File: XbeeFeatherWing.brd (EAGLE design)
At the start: 124.5 x 66 mm, 18 parts, among them U2 XBEE-1B3

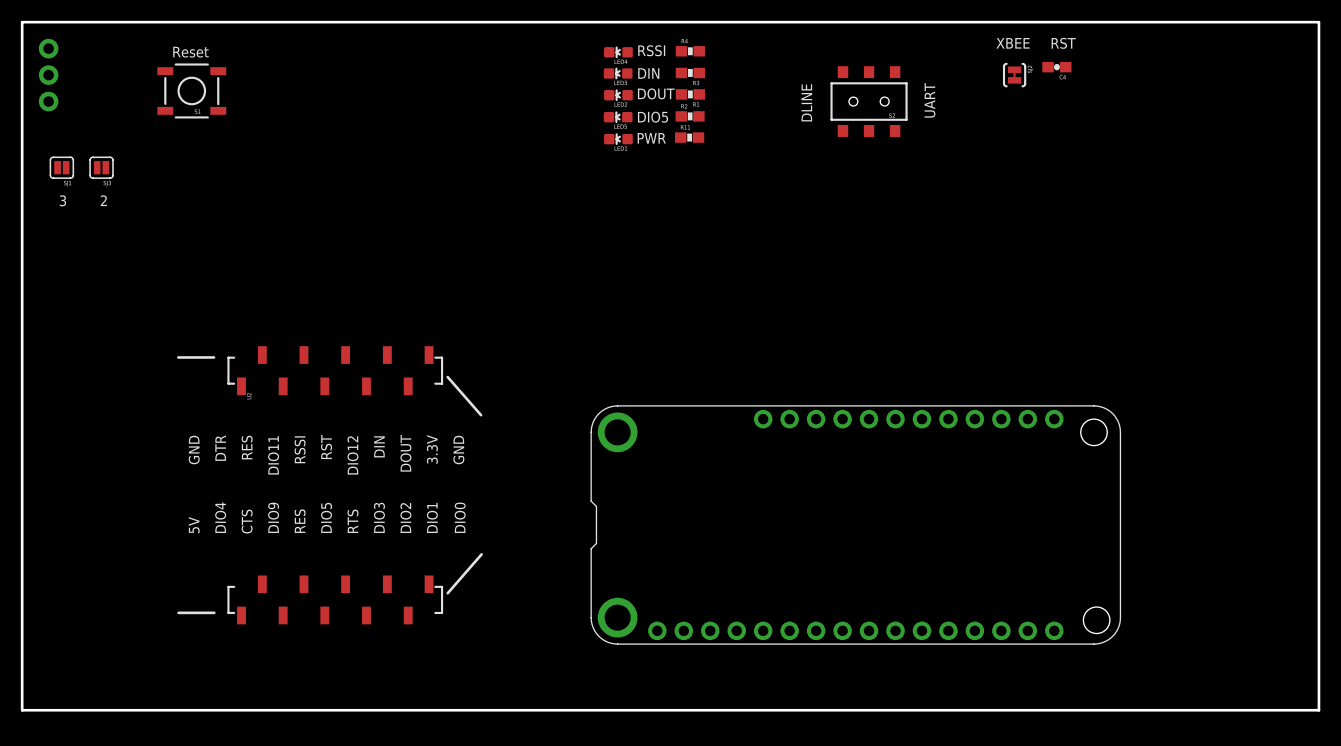
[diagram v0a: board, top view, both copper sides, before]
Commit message: changed xbee to adafruit footprint
the sparkfun footprint was smd, needed THT pins
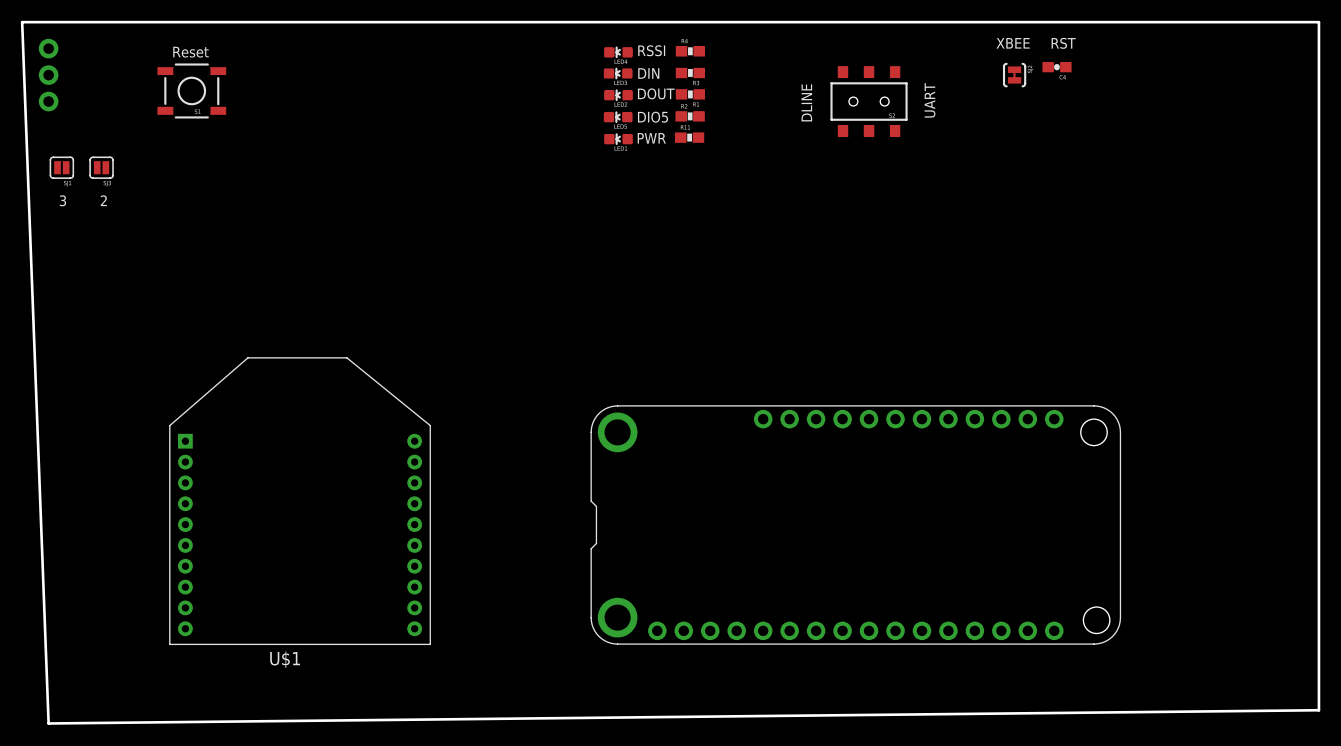
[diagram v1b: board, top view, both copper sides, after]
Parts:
- removed U2: XBEE-1B3, SparkFun:XBEE-SMD
- added U$1: XBEE, adafruit:XBEE
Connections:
- new net N$8: U$1.17
- net 3.3V: now also U$1.1; no longer U2.1
- net DIN: now also U$1.3; no longer U2.3
- net DIO3: no longer U2.17
- net DIO5: now also U$1.15; no longer U2.15
- net DOUT: now also U$1.2; no longer U2.2
- net GND: now also U$1.10; no longer U2.10
- net RSSI: now also U$1.6; no longer U2.6
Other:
- board size 124.5 x 66 mm -> 124.5 x 67.3 mm
- board text removed: "3.3V"
- board text removed: "5V"
- board text removed: "CTS"
- board text removed: "DIO0"
- board text removed: "DIO1"
- board text removed: "DIO11"
- board text removed: "DIO12"
- board text removed: "DIO2"
- board text removed: "DIO3"
- board text removed: "DIO4"
- board text removed: "DIO9"
- board text removed: "DTR"
- board text removed: "GND"
- board text removed: "RES"
- board text removed: "RTS"
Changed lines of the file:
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@@
 <board>
 <plain>
-<wire x1="0" y1="-6.35" x2="0" y2="59.69" width="0.254" layer="20"/>
+<wire x1="2.54" y1="-7.62" x2="0" y2="59.69" width="0.254" layer="20"/>
 <wire x1="0" y1="59.69" x2="124.46" y2="59.69" width="0.254" layer="20"/>
 <wire x1="124.46" y1="59.69" x2="124.46" y2="-6.35" width="0.254" layer="20"/>
-<wire x1="124.46" y1="-6.35" x2="0" y2="-6.35" width="0.254" layer="20"/>
-<wire x1="40.8432" y1="25.6286" x2="44.0436" y2="21.971" width="0.254" layer="21"/>
-<wire x1="40.8432" y1="4.8768" x2="44.0944" y2="8.6106" width="0.254" layer="21"/>
-<wire x1="18.4404" y1="2.9972" x2="15.0114" y2="2.9972" width="0.254" layer="21"/>
-<wire x1="18.415" y1="27.5082" x2="14.986" y2="27.5082" width="0.254" layer="21"/>
-<text x="42.545" y="10.541" size="1.016" layer="21" font="vector" ratio="15" rot="R90">DIO0</text>
-<text x="39.878" y="10.541" size="1.016" layer="21" font="vector" ratio="15" rot="R90">DIO1</text>
-<text x="37.338" y="10.541" size="1.016" layer="21" font="vector" ratio="15" rot="R90">DIO2</text>
-<text x="34.798" y="10.541" size="1.016" layer="21" font="vector" ratio="15" rot="R90">DIO3</text>
-<text x="32.258" y="10.541" size="1.016" layer="21" font="vector" ratio="15" rot="R90">RTS</text>
-<text x="29.718" y="10.541" size="1.016" layer="21" font="vector" ratio="15" rot="R90">DIO5</text>
-<text x="27.178" y="10.541" size="1.016" layer="21" font="vector" ratio="15" rot="R90">RES</text>
-<text x="24.638" y="10.541" size="1.016" layer="21" font="vector" ratio="15" rot="R90">DIO9</text>
-<text x="22.098" y="10.541" size="1.016" layer="21" font="vector" ratio="15" rot="R90">CTS</text>
-<text x="19.558" y="10.541" size="1.016" layer="21" font="vector" ratio="15" rot="R90">DIO4</text>
-<text x="17.018" y="10.541" size="1.016" layer="21" font="vector" ratio="15" rot="R90">5V</text>
-<text x="16.002" y="20.066" size="1.016" layer="21" font="vector" ratio="15" rot="R270">GND</text>
-<text x="18.542" y="20.066" size="1.016" layer="21" font="vector" ratio="15" rot="R270">DTR</text>
-<text x="21.082" y="20.066" size="1.016" layer="21" font="vector" ratio="15" rot="R270">RES</text>
-<text x="23.622" y="20.066" size="1.016" layer="21" font="vector" ratio="15" rot="R270">DIO11</text>
-<text x="26.162" y="20.066" size="1.016" layer="21" font="vector" ratio="15" rot="R270">RSSI</text>
-<text x="28.702" y="20.066" size="1.016" layer="21" font="vector" ratio="15" rot="R270">RST</text>
-<text x="31.242" y="20.066" size="1.016" layer="21" font="vector" ratio="15" rot="R270">DIO12</text>
-<text x="33.782" y="20.066" size="1.016" layer="21" font="vector" ratio="15" rot="R270">DIN</text>
-<text x="36.322" y="20.066" size="1.016" layer="21" font="vector" ratio="15" rot="R270">DOUT</text>
-<text x="38.862" y="20.066" size="1.016" layer="21" font="vector" ratio="15" rot="R270">3.3V</text>
-<text x="41.402" y="20.066" size="1.016" layer="21" font="vector" ratio="15" rot="R270">GND</text>
+<wire x1="124.46" y1="-6.35" x2="2.54" y2="-7.62" width="0.254" layer="20"/>
 <text x="59.0042" y="56.4388" size="1.016" layer="21" font="vector" ratio="15" rot="SR0">RSSI</text>
 <text x="59.0042" y="54.2544" size="1.016" layer="21" font="vector" ratio="15" rot="SR0">DIN</text>
@@
 <attribute name="VALUE" value="1K" x="64.135" y="54.8132" size="1.778" layer="27" rot="R180" display="off"/>
 </element>
-<element name="U2" library="SparkFun" package="XBEE-SMD" value="XBEE-1B3" x="19.05" y="15.24" rot="R270"/>
 <element name="LED4" library="SparkFun-LED" package="LED-0603" value="Green" x="57.2262" y="56.7944" rot="R90">
 <attribute name="PROD_ID" value="DIO-00821" x="57.2262" y="56.7944" size="1.778" layer="27" rot="R90" display="off"/>
@@
 <element name="SJ3" library="SparkFun" package="SJ_2S" value="D_RX" x="7.62" y="45.72" rot="R180"/>
 <element name="MS2" library="Proto FeatherWing" package="MICROSHIELD_DIM" value="MICROSHIELD_NODIM" x="54.61" y="0"/>
+<element name="U$1" library="adafruit" package="XBEE" value="XBEE" x="26.67" y="13.97"/>
 </elements>
 <signals>
@@
 <contactref element="MS2" pad="4"/>
 <contactref element="MS2" pad="27"/>
-<contactref element="U2" pad="10"/>
+<contactref element="U$1" pad="10"/>
 <wire x1="56.3238" y1="50.5714" x2="56.3492" y2="56.7944" width="0" layer="19" extent="1-1"/>
 <wire x1="56.3492" y1="48.4632" x2="56.3238" y2="50.5714" width="0" layer="19" extent="1-1"/>
@@
 <wire x1="68.58" y1="1.27" x2="73.66" y2="21.59" width="0" layer="19" extent="1-1"/>
 <wire x1="18.8214" y1="51.181" x2="56.3238" y2="50.5714" width="0" layer="19" extent="1-1"/>
-<wire x1="21.05" y1="24.74" x2="18.8214" y2="51.181" width="0" layer="19" extent="1-1"/>
+<wire x1="15.67" y1="1.47" x2="18.8214" y2="51.181" width="0" layer="19" extent="1-1"/>
 </signal>
 <signal name="N$38">
@@
 <signal name="DIN">
 <contactref element="LED3" pad="C"/>
-<contactref element="U2" pad="3"/>
 <contactref element="S2" pad="5"/>
+<contactref element="U$1" pad="3"/>
 <wire x1="56.3238" y1="54.7624" x2="81.28" y2="54.895" width="0" layer="19" extent="1-1"/>
-<wire x1="35.05" y1="27.74" x2="56.3238" y2="54.7624" width="0" layer="19" extent="1-1"/>
+<wire x1="15.67" y1="15.47" x2="56.3238" y2="54.7624" width="0" layer="19" extent="1-1"/>
 </signal>
 <signal name="DOUT">
 <contactref element="LED2" pad="C"/>
-<contactref element="U2" pad="2"/>
 <contactref element="S2" pad="2"/>
+<contactref element="U$1" pad="2"/>
 <wire x1="56.3492" y1="52.6796" x2="81.28" y2="49.245" width="0" layer="19" extent="1-1"/>
-<wire x1="37.05" y1="24.74" x2="56.3492" y2="52.6796" width="0" layer="19" extent="1-1"/>
+<wire x1="15.67" y1="17.47" x2="56.3492" y2="52.6796" width="0" layer="19" extent="1-1"/>
 </signal>
 <signal name="3.3V">
-<contactref element="U2" pad="1"/>
 <contactref element="R11" pad="2"/>
 <contactref element="R3" pad="1"/>
 <contactref element="R1" pad="1"/>
 <contactref element="MS2" pad="2"/>
+<contactref element="U$1" pad="1"/>
 <wire x1="64.985" y1="52.7558" x2="64.985" y2="54.8132" width="0" layer="19" extent="1-1"/>
 <wire x1="64.9088" y1="48.6156" x2="64.985" y2="52.7558" width="0" layer="19" extent="1-1"/>
-<wire x1="39.05" y1="27.74" x2="64.9088" y2="48.6156" width="0" layer="19" extent="1-1"/>
-<wire x1="63.5" y1="1.27" x2="39.05" y2="27.74" width="0" layer="19" extent="1-1"/>
+<wire x1="63.5" y1="1.27" x2="64.9088" y2="48.6156" width="0" layer="19" extent="1-1"/>
+<wire x1="15.67" y1="19.47" x2="63.5" y2="1.27" width="0" layer="19" extent="1-1"/>
 </signal>
 <signal name="DIO5">
-<contactref element="U2" pad="15"/>
 <contactref element="R2" pad="2"/>
-<wire x1="29.05" y1="2.74" x2="64.9596" y2="50.6476" width="0" layer="19" extent="1-1"/>
+<contactref element="U$1" pad="15"/>
+<wire x1="37.67" y1="9.47" x2="64.9596" y2="50.6476" width="0" layer="19" extent="1-1"/>
 </signal>
 <signal name="DIO3">
-<contactref element="U2" pad="17"/>
 <contactref element="SJ2" pad="2"/>
-<wire x1="33.05" y1="2.74" x2="95.25" y2="54.102" width="0" layer="19" extent="1-1"/>
 </signal>
 <signal name="RSSI">
-<contactref element="U2" pad="6"/>
 <contactref element="R4" pad="2"/>
-<wire x1="29.05" y1="24.74" x2="64.985" y2="56.896" width="0" layer="19" extent="1-1"/>
+<contactref element="U$1" pad="6"/>
+<wire x1="15.67" y1="9.47" x2="64.985" y2="56.896" width="0" layer="19" extent="1-1"/>
 </signal>
 <signal name="N$2">
@@
 <contactref element="C4" pad="1"/>
 <contactref element="MS2" pad="1"/>
-<wire x1="18.8214" y1="54.991" x2="100.164" y2="55.372" width="0" layer="19" extent="1-1"/>
-<wire x1="60.96" y1="1.27" x2="18.8214" y2="54.991" width="0" layer="19" extent="1-1"/>
+<wire x1="60.96" y1="1.27" x2="100.164" y2="55.372" width="0" layer="19" extent="1-1"/>
+<wire x1="18.8214" y1="54.991" x2="60.96" y2="1.27" width="0" layer="19" extent="1-1"/>
 </signal>
 <signal name="N$5">
@@
 <contactref element="S2" pad="1"/>
 <contactref element="MS2" pad="14"/>
-<wire x1="83.78" y1="49.245" x2="93.98" y2="1.27" width="0" layer="19" extent="1-1"/>
+<wire x1="93.98" y1="1.27" x2="83.78" y2="49.245" width="0" layer="19" extent="1-1"/>
 </signal>
 <signal name="UART_TX">
 <contactref element="S2" pad="4"/>
 <contactref element="MS2" pad="15"/>
-<wire x1="83.78" y1="54.895" x2="96.52" y2="1.27" width="0" layer="19" extent="1-1"/>
+<wire x1="96.52" y1="1.27" x2="83.78" y2="54.895" width="0" layer="19" extent="1-1"/>
 </signal>
 <signal name="N$140">
@@
 <wire x1="7.2081" y1="45.72" x2="78.78" y2="49.245" width="0" layer="19" extent="1-1"/>
 </signal>
+<signal name="N$8">
+<contactref element="U$1" pad="17"/>
+</signal>
 </signals>

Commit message: v1 of the board with layout complete
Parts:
- moved SJ1 92.9 mm to (94.6, 26.0)
- moved SJ3 89.8 mm to (94.6, 23.5)
- moved S1 85.1 mm to (93.0, 16.3), turned to 270 degrees
- moved U$1 49.6 mm to (76.2, 16.5), turned to 270 degrees
- moved S2 44.6 mm to (55.2, 15.9)
- moved R4 34.3 mm to (60.1, 22.9), turned to 270 degrees
- moved R3 32.5 mm to (58.0, 22.9), turned to 90 degrees
- moved R1 31.0 mm to (55.9, 22.9), turned to 90 degrees
- moved C4 30.9 mm to (86.7, 27.2), turned to 90 degrees
- moved R2 29.6 mm to (53.8, 22.9), turned to 270 degrees
- moved R11 28.5 mm to (51.8, 22.9), turned to 270 degrees
- moved SJ2 27.3 mm to (89.5, 27.9), turned to 180 degrees
- moved LED4 27.2 mm to (60.0, 29.8), turned to 0 degrees
- moved LED3 25.0 mm to (57.9, 29.8), turned to 0 degrees
- moved LED2 23.0 mm to (55.9, 29.8), turned to 0 degrees
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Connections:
- removed net N$8: U$1.17
- net DIO3: now also U$1.17
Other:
- board text added: "5"
- board text added: "6"
- board text added: "DLINE uses pins D5 for RX and D6 for TX Solder jumper cable to use different pins Solder XBEE RST to connectio to DIO13 on XBEE Reset wired to arduino reset not XBEE"
- board text added: "Perednik"
- board text added: "v1.0"
- board text added: "xBee FeatherWing"
- board text added: "xBee FeatherWing v1.0"
- board text removed: "2"
- board text removed: "3"

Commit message: routing complete
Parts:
- SJ2: value SOLDERJUMPERTRACE -> SOLDERJUMPERNC; device SparkFun:SJ_2S-TRACE -> SparkFun-Retired:SJ_2S
- moved SJ2 22.2 mm to (89.5, 5.71)
- moved C4 21.1 mm to (92.5, 6.86), turned to 225 degrees
- moved LED1 4.45 mm to (56.1, 29.8)
- moved LED5 4.45 mm to (58.2, 29.8)
- moved R11 4.45 mm to (56.2, 22.9)
- moved R2 4.45 mm to (58.3, 22.9)
- moved R3 3.81 mm to (54.2, 22.9)
- moved LED2 3.81 mm to (52.0, 29.8)
- moved LED3 3.81 mm to (54.1, 29.8)
- moved R1 3.81 mm to (52.1, 22.9)
- turned S1 to 90 degrees
- turned SJ1 to 270 degrees
- turned SJ3 to 270 degrees
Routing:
- net GND: track 0.00 -> 73.1 mm
- net 3.3V: track 0.00 -> 61.7 mm
- net DOUT: track 0.00 -> 60.5 mm, vias 0 -> 1
- net RST: track 0.00 -> 49.7 mm, vias 0 -> 1
- net N$141: track 0.00 -> 47.3 mm, vias 0 -> 2
- net UART_TX: track 0.00 -> 45.4 mm
- net N$140: track 0.00 -> 45.4 mm, vias 0 -> 2
- net DIN: track 0.00 -> 35.9 mm, vias 0 -> 2
- net UART_RX: track 0.00 -> 28.5 mm, vias 0 -> 1
- net DIO5: track 0.00 -> 23.1 mm
- net D_TX: track 0.00 -> 21.2 mm
- net DIO3: track 0.00 -> 14.7 mm, vias 0 -> 1
- net RSSI: track 0.00 -> 13.9 mm
- net D_RX: track 0.00 -> 12.2 mm
- net N$139: track 0.00 -> 5.34 mm
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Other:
- board size 124.5 x 67.3 mm -> 50.9 x 28.6 mm
